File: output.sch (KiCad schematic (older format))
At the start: 36 parts, among them SW1 1AS2T2B4M2RE, U11 TC7650, U12 TC7650, U13 DG419, U14 TC7650

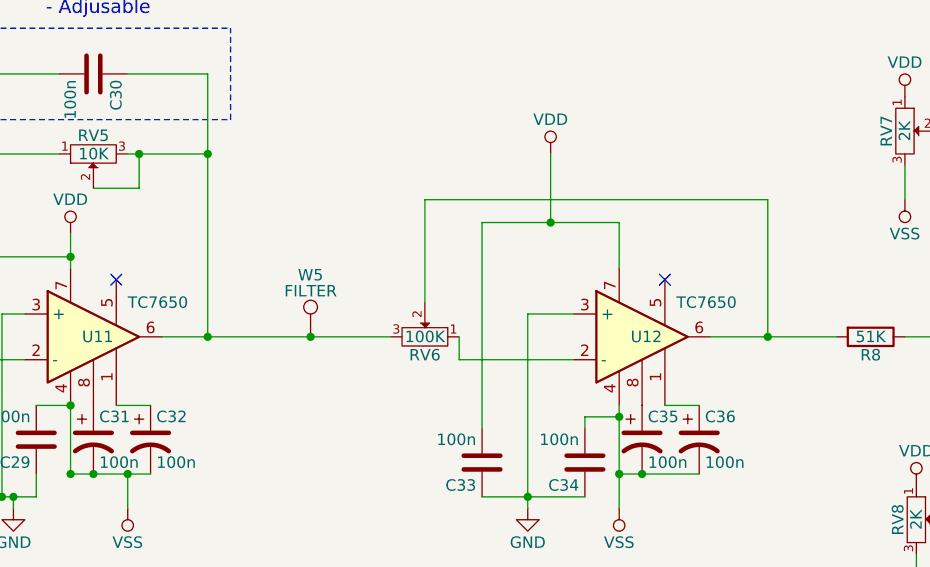
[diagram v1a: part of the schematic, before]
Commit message: Documented and fixed output gain bug
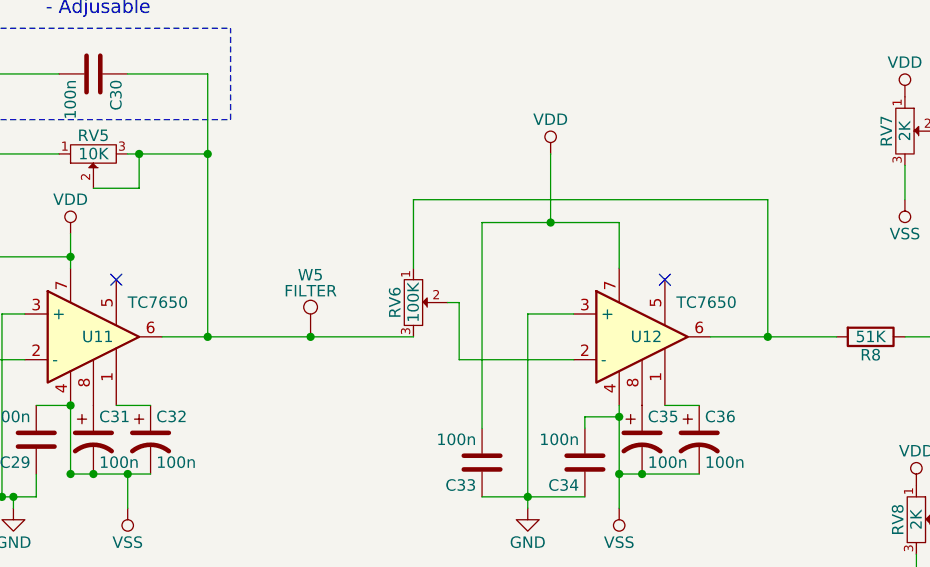
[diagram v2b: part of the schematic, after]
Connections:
- net at U12.2 (-): now also RV6.2; no longer RV6.1
- net at R8.2, U12.6: now also RV6.1; no longer RV6.2
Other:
- moved on the sheet: RV6
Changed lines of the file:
@@
 Sheet 3 3
 Title "Helmholtz Current Servo"
-Date "2016-11-14"
+Date "2016-12-15"
 Rev ""
 Comp "Kjaergaard Lab"
@@
 L POT RV6
 U 1 1 5820ECF5
-P 3450 4050
-F 0 "RV6" H 3450 3970 50  0000 C CNN
-F 1 "100K" H 3450 4050 50  0000 C CNN
-F 2 "Potentiometers:Potentiometer_Bourns_3296W_3-8Zoll_Inline_ScrewUp" H 3450 4050 50  0001 C CNN
-F 3 "" H 3450 4050 50  0000 C CNN
-	1    3450 4050
-	-1   0    0    -1
+P 3400 3900
+F 0 "RV6" H 3400 3820 50  0000 C CNN
+F 1 "100K" H 3400 3900 50  0000 C CNN
+F 2 "Potentiometers:Potentiometer_Bourns_3296W_3-8Zoll_Inline_ScrewUp" H 3400 3900 50  0001 C CNN
+F 3 "" H 3400 3900 50  0000 C CNN
+	1    3400 3900
+	0    1    1    0
 $EndComp
 $Comp
@@
 Connection ~ 4000 3550
 Wire Wire Line
-	3600 4050 3600 4150
+	3600 3900 3600 4150
 Wire Wire Line
 	3600 4150 4100 4150
 Wire Wire Line
-	4950 4050 4950 3450
-Wire Wire Line
-	4950 3450 3450 3450
-Wire Wire Line
-	3450 3450 3450 3900
+	4950 3450 4950 4050
+Wire Wire Line
+	3400 3450 4950 3450
 Wire Wire Line
 	6250 3150 5700 3150
@@
 Connection ~ 1400 3250
 Wire Wire Line
-	2300 4050 3300 4050
+	2300 4050 3400 4050
 Wire Wire Line
 	1050 3750 1400 3750
@@
 $EndComp
 Connection ~ 6850 3150
+Wire Wire Line
+	3550 3900 3600 3900
+Wire Wire Line
+	3400 3450 3400 3750
 $EndSCHEMATC
